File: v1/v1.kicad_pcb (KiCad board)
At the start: 2 copper layers, 101.5 x 105.4 mm, 61 parts, among them CON1 SNES-CONN

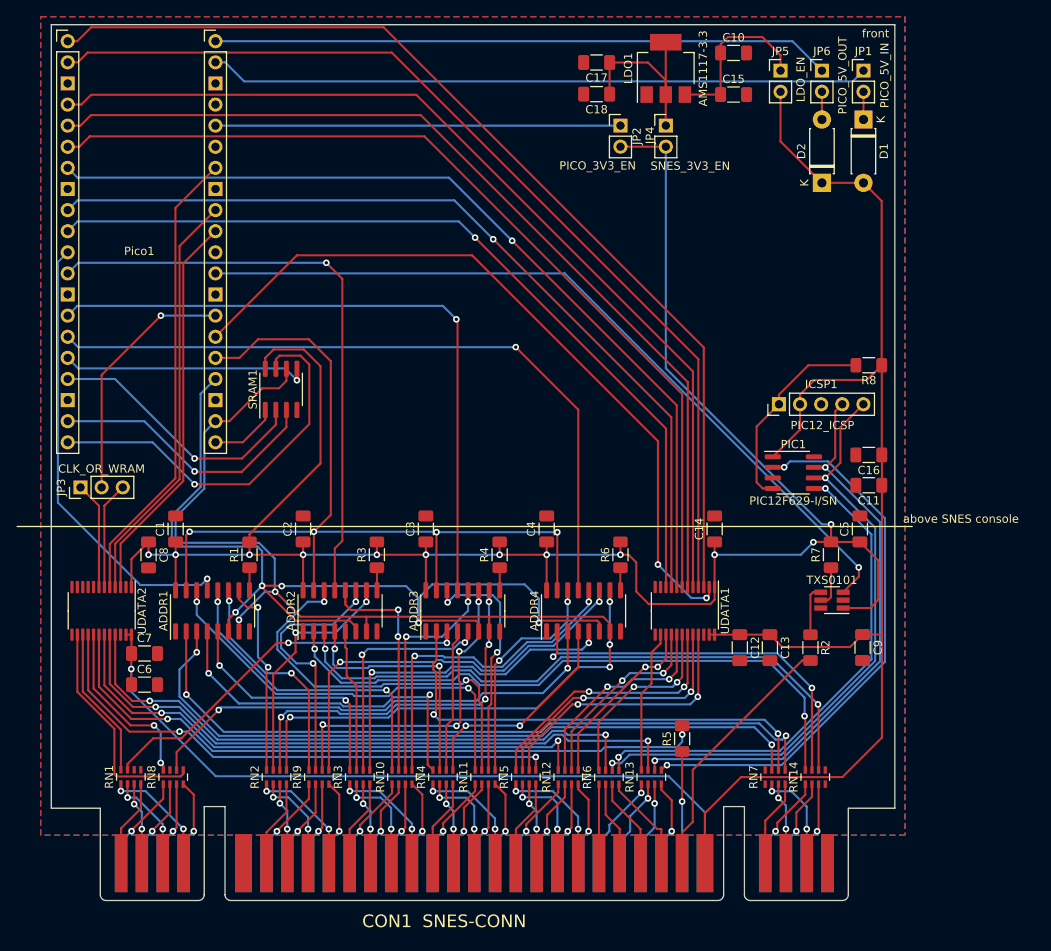
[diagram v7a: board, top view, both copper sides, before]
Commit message: v1: added jumper and diode for SNES 5V supply feeding +5V rail
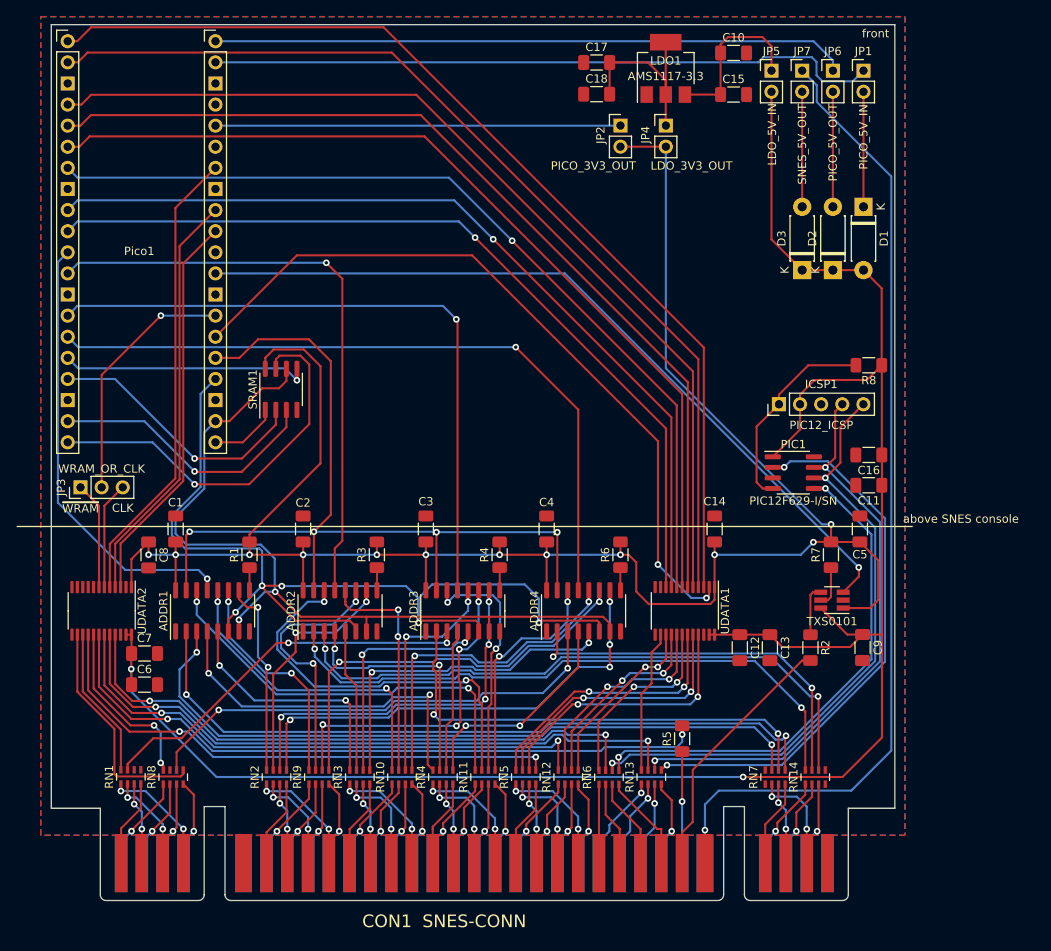
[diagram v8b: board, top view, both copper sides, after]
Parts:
- added D3: 1N5818, Diode_THT:D_DO-41_SOD81_P7.62mm_Horizontal, F.Cu at (176.6, 58.0)
- added JP7: SNES_5V_OUT, Connector_PinHeader_2.54mm:PinHeader_1x02_P2.54mm_Vertical, F.Cu at (176.6, 34.0)
- JP2: value PICO_3V3_EN -> PICO_3V3_OUT
- JP3: value CLK_OR_WRAM -> WRAM_OR_CLK
- JP4: value SNES_3V3_EN -> LDO_3V3_OUT
- JP5: value LDO_EN -> LDO_5V_IN
- moved D2 10.6 mm to (180.3, 58.0)
- moved D1 10.5 mm to (184.0, 50.4)
- moved JP6 1.32 mm to (180.3, 34.0)
- moved JP5 1.09 mm to (172.9, 34.0)
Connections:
- CON1 pad 27: +5V -> Net-(CON1-Pad27)
- CON1 pad 58: +5V -> Net-(CON1-Pad27)
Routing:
- net Net-(CON1-Pad27): track 0.00 -> 122.4 mm, vias 0 -> 1
- net Net-(JP7-Pad2): track 0.00 -> 13.8 mm
- net Net-(D2-Pad2): track 3.34 -> 13.8 mm
- net Net-(D1-Pad1): track 3.34 -> 13.8 mm
- net +5V: track 249.1 -> 241.6 mm, vias 1 -> 2
- net Net-(JP6-Pad1): track 74.4 -> 76.5 mm
- net /YPA1: track 76.1 -> 74.3 mm
- net Net-(JP1-Pad1): track 79.5 -> 80.9 mm
- net /ADDR1QH: track 54.4 -> 53.8 mm
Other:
- board text added: "CLK"
- board text added: "~{WRAM}"
